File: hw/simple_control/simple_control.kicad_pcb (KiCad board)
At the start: 4 copper layers, 80 x 100 mm, 105 parts, among them J101 Screw_Terminal_01x02, J102 Jack-DC, J103 Screw_Terminal_01x03, J104 Screw_Terminal_01x03, J1301 Micro_SD_Card, J1401 Conn_02x05_Odd_Even, J601 Conn_01x04, J602 Raspberry_Pi_0_2_3, J603 Conn_01x03, Q1001 BC817, Q201 AOSP21357, Q701 BC817, Q801 BC817, Q901 BC817, SW1801 SW_Push, SW1901 SW_Push, SW2001 SW_Push, SW2101 SW_Push, SW602 SW_Push, U1101 CAT24C256, U1501 4050, U301 SN74AHCT125D, U601 PicoW

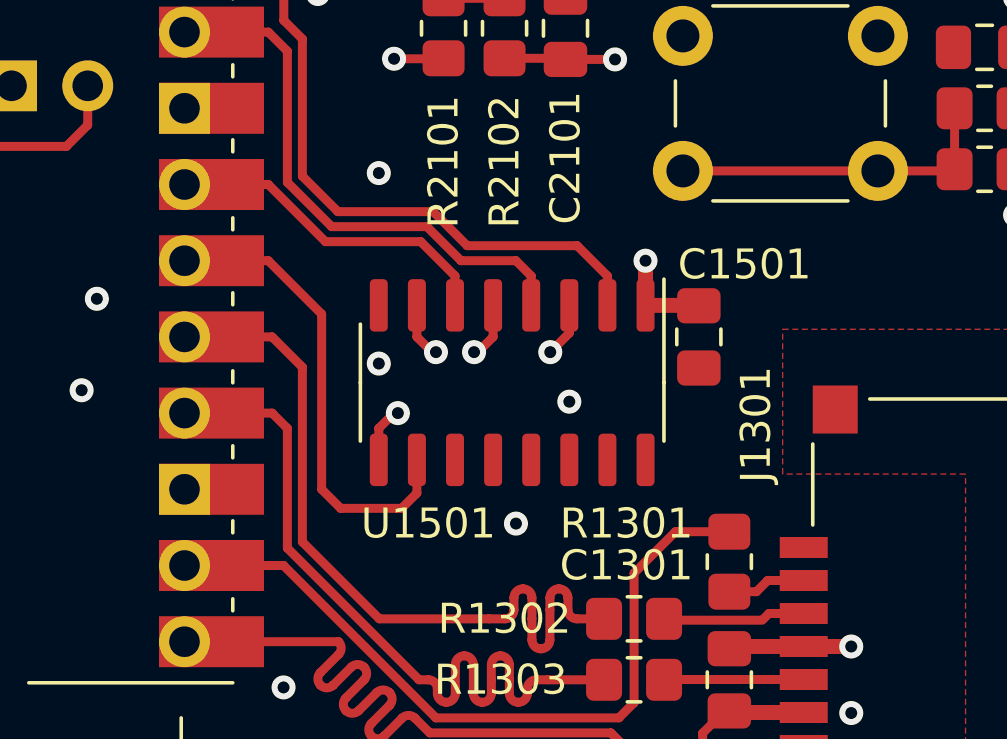
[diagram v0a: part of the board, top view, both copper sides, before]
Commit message: chore(hw): switch to 74AHC125 for keypad buffer
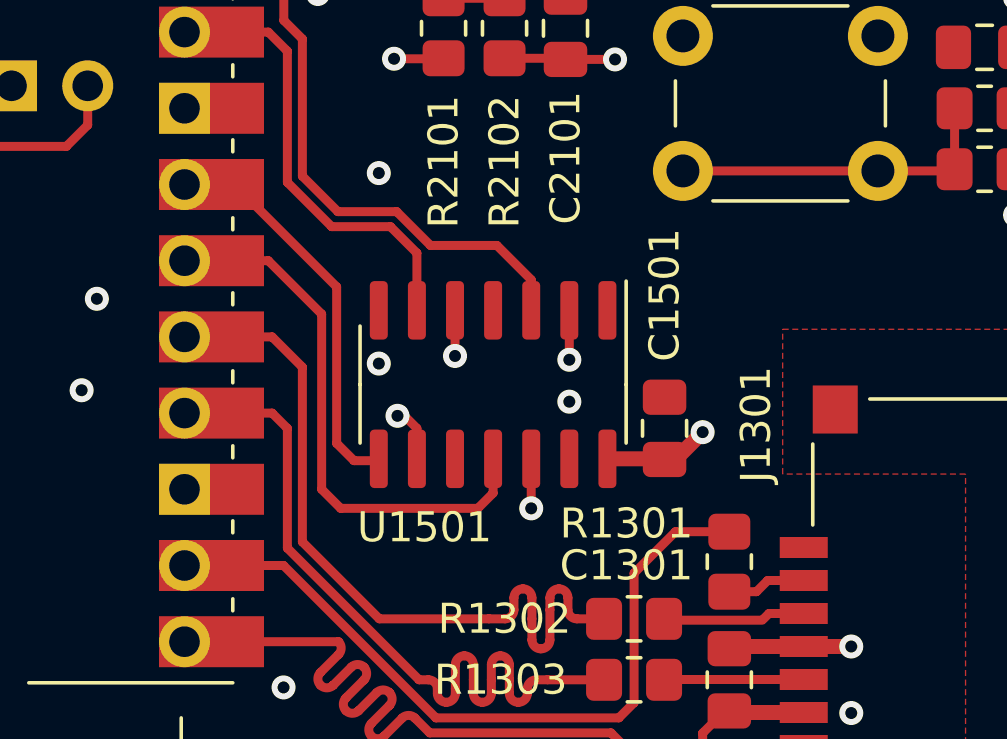
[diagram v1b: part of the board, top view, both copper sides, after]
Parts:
- U1501: value 4050 -> 74AHC125; footprint Package_SO:SO-16_3.9x9.9mm_P1.27mm -> Package_SO:SO-14_3.9x8.65mm_P1.27mm
- moved C1501 3.26 mm to (158.9, 96.3), turned to 90 degrees
- moved U1501 0.64 mm to (153.2, 94.8)
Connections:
- U1501 pad 1: +3.3V -> GND
- U1501 pad 10: /CPU/BUTTON3 -> GND
- U1501 pad 11: GND -> /CPU/BUTTON3
- U1501 pad 12: unconnected-(U1501-Pad12) -> /CPU/Keypad/Filtered Button 3/SW
- U1501 pad 13: (no net) -> GND
- U1501 pad 14: GND -> +3.3V
- U1501 pad 2: /CPU/BUTTON0 -> /CPU/Keypad/Filtered Button 0/SW
- U1501 pad 3: /CPU/Keypad/Filtered Button 0/SW -> /CPU/BUTTON0
- U1501 pad 4: /CPU/BUTTON1 -> GND
- U1501 pad 6: /CPU/BUTTON2 -> /CPU/BUTTON1
- U1501 pad 7: /CPU/Keypad/Filtered Button 2/SW -> GND
- U1501 pad 8: GND -> /CPU/BUTTON2
- U1501 pad 9: /CPU/Keypad/Filtered Button 3/SW -> /CPU/Keypad/Filtered Button 2/SW
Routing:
- net /CPU/Keypad/Filtered Button 3/SW: track 20.4 -> 27.6 mm
- net /CPU/BUTTON1: track 47.0 -> 43.9 mm
- net /CPU/Keypad/Filtered Button 2/SW: track 31.1 -> 33.7 mm
- net /CPU/BUTTON3: track 51.7 -> 54.2 mm
- net /CPU/BUTTON0: track 67.4 -> 65.0 mm
- net /CPU/BUTTON2: track 38.8 -> 40.8 mm
- net GND: vias 50 -> 49

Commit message: chore(hw): minor layout fixes, add notes
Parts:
- moved U1501 0.06 mm to (153.2, 94.9)
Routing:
- net GND: vias 49 -> 51

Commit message: chore(hw): improve layout
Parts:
- moved C1402 0.76 mm to (153.0, 48.1)
- moved C1401 0.63 mm to (153.0, 45.8)
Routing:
- net GND: track 110.1 -> 122.5 mm, vias 51 -> 53
- net /CPU/TERM_TXD: track 87.3 -> 97.6 mm
- net Net-(U301-3~{OE}): track 16.9 -> 21.6 mm
- net /CPU/TERM_RXD: track 82.8 -> 79.6 mm
- net +5V: track 49.4 -> 51.9 mm
- net Net-(U301-1~{OE}): track 19.7 -> 21.9 mm, vias 0 -> 2
- net /CPU/STAT_LED3: track 88.0 -> 89.2 mm
- net /LED_DATA_~{EN}0: track 85.8 -> 86.4 mm
- net /CPU/RTC_SDA: track 61.3 -> 61.9 mm
- net /CPU/RTC_SCL: track 66.0 -> 66.6 mm
- net /CPU/STAT_LED2: track 92.8 -> 93.4 mm
- net /CPU/STAT_LED1: track 82.4 -> 83.0 mm
- net /CPU/STAT_LED0: track 86.5 -> 87.1 mm
- net Net-(U301-3A): track 14.6 -> 14.2 mm, vias 2 -> 0
- net Net-(U301-1A): track 14.8 -> 15.0 mm, vias 2 -> 0

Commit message: chore(hw): add JLC order number
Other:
- board text added: "JLCJLCJLCJLC"
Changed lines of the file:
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@@
   (gr_line (start 108.1 140.64) (end 175.1 140.64)
     (stroke (width 0.1) (type default)) (layer "Edge.Cuts"))
+  (gr_text "JLCJLCJLCJLC" (at 158.369 132.207) (layer "F.SilkS")
+    (effects (font (size 1 1) (thickness 0.15)) (justify left bottom))
+  )
   (dimension (type aligned) (layer "Eco1.User")
     (pts (xy 108.1 40.64) (xy 108.1 140.64))

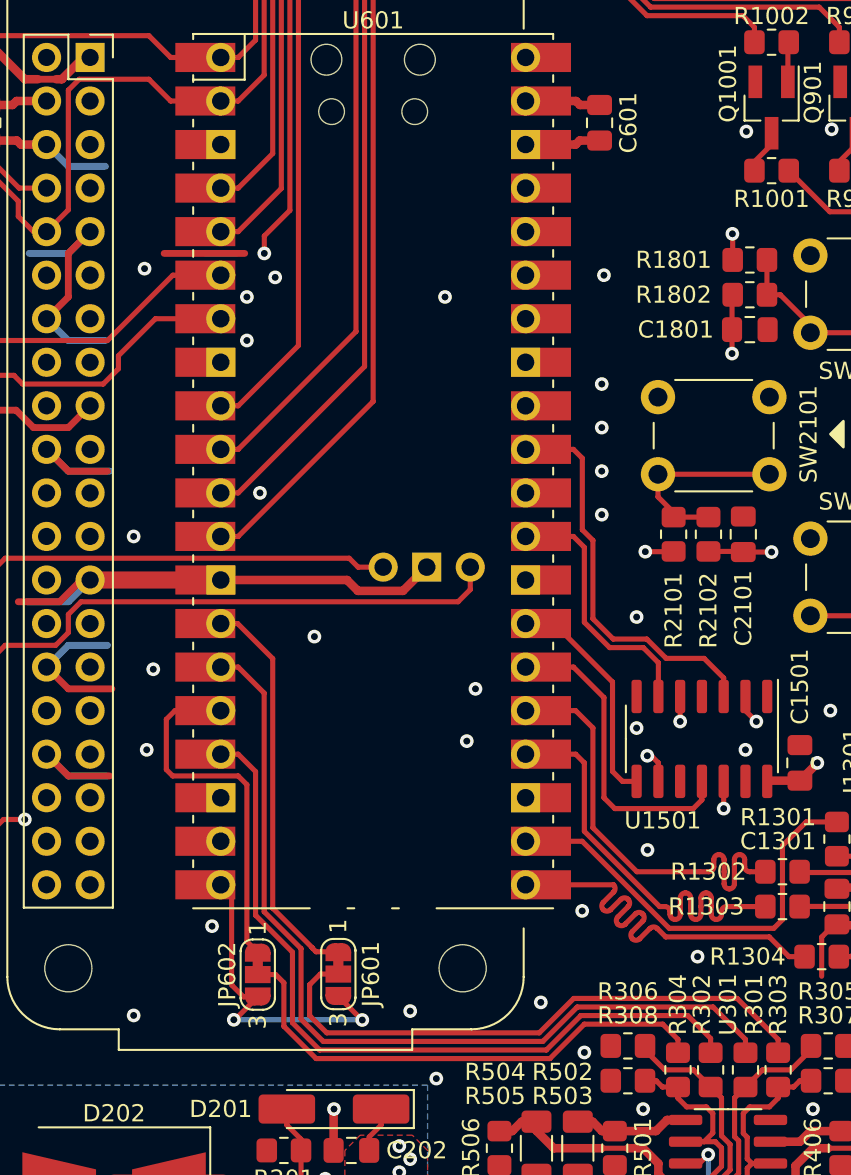
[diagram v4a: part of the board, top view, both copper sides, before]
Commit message: chore(hw): move LED data outside of antenna keep-out area
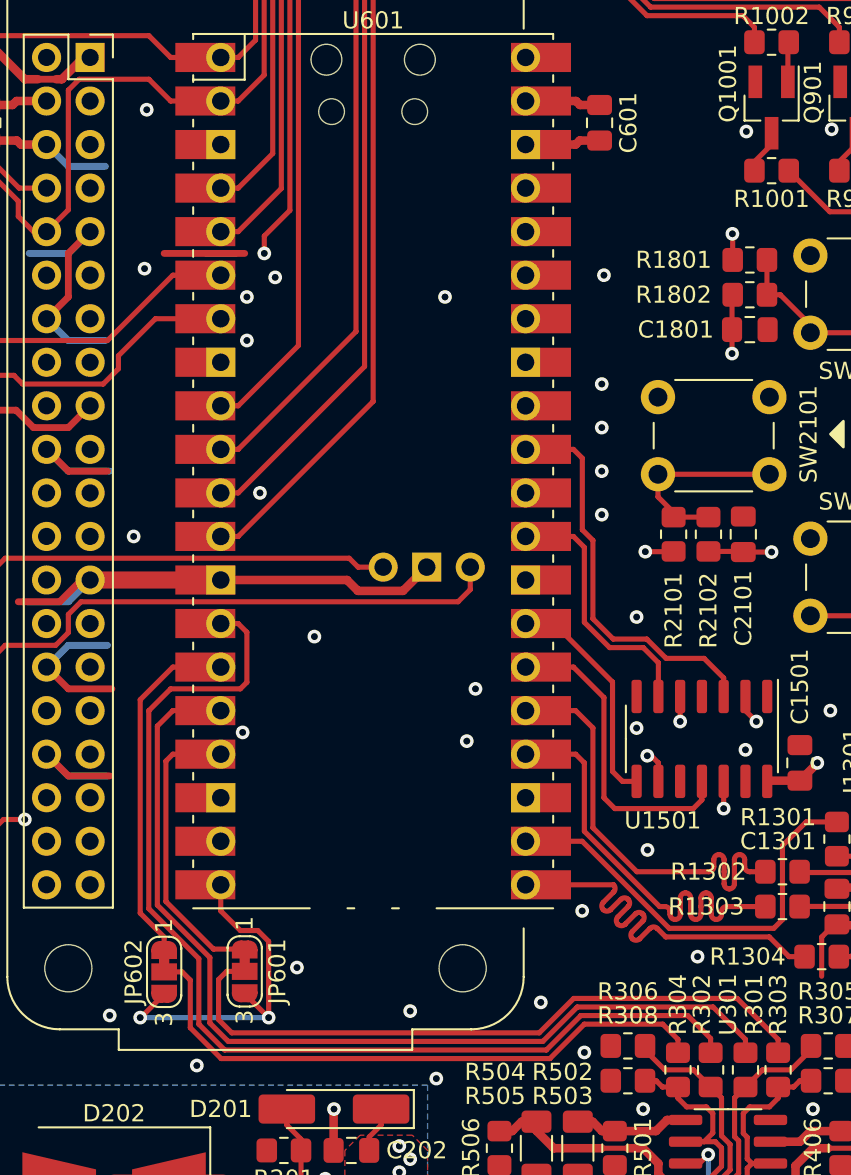
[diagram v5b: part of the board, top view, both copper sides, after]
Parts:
- moved JP601 5.46 mm to (126.5, 108.4)
- moved JP602 5.46 mm to (121.8, 108.5)
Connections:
- U601 pad 14: /CPU/PRIM_LED_DATA0 -> /LED_DATA_~{EN}1
- U601 pad 15: /LED_DATA_~{EN}0 -> /CPU/PRIM_LED_DATA1
- U601 pad 16: /CPU/PRIM_LED_DATA1 -> /LED_DATA_~{EN}0
- U601 pad 17: /LED_DATA_~{EN}1 -> /CPU/PRIM_LED_DATA0
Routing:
- net /LED_DATA_~{EN}1: track 56.5 -> 86.8 mm
- net /LED_DATA_~{EN}0: track 86.4 -> 93.8 mm
- net /LED_DATA1: track 30.0 -> 35.7 mm
- net /LED_DATA0: track 34.1 -> 39.6 mm
- net /CPU/PRIM_LED_DATA0: track 35.6 -> 30.7 mm
- net /CPU/PRIM_LED_DATA1: track 30.1 -> 34.0 mm
- net /CPU/ALT_LED_DATA: track 30.5 -> 32.1 mm
- net GND: vias 53 -> 54

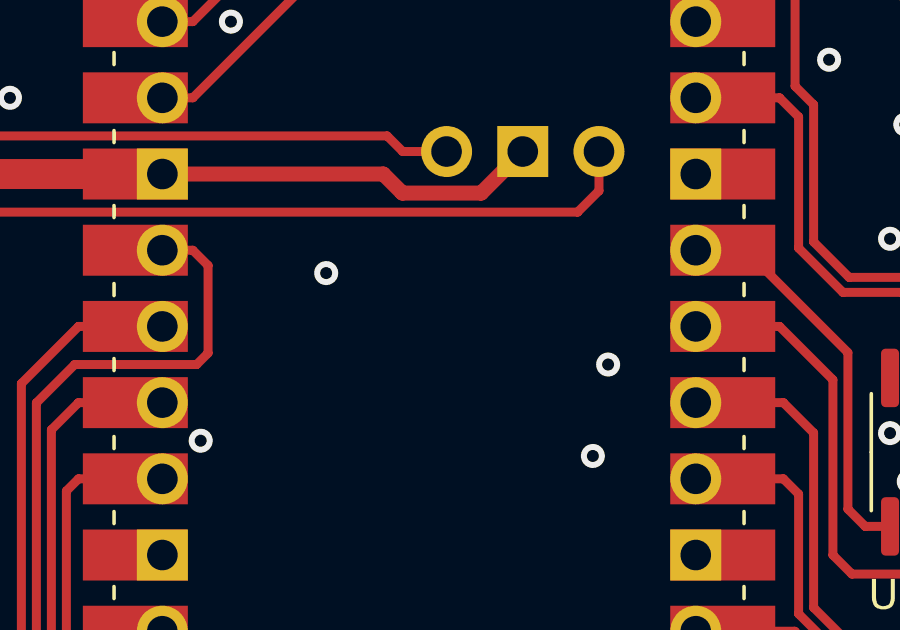
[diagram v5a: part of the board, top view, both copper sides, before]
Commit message: chore(hw): move vias under RPi
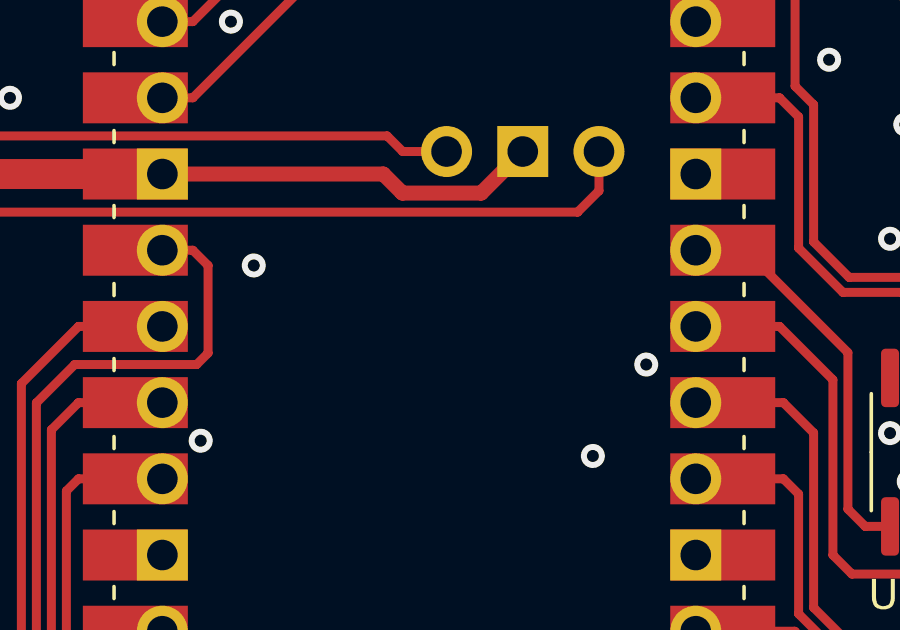
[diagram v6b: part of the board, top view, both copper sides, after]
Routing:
- net Net-(U601-RUN): track 54.1 -> 54.8 mm
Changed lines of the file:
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@@
   (via (at 165.1 105.7556) (size 0.8) (drill 0.4) (layers "F.Cu" "B.Cu") (free) (net 2))
   (via (at 165.6588 59.309) (size 0.8) (drill 0.4) (layers "F.Cu" "B.Cu") (free) (net 2))
-  (via (at 130.556 88.9) (size 0.8) (drill 0.4) (layers "F.Cu" "B.Cu") (free) (net 2))
+  (via (at 128.143 88.646) (size 0.8) (drill 0.4) (layers "F.Cu" "B.Cu") (free) (net 2))
   (via (at 162.814 77.089) (size 0.8) (drill 0.4) (layers "F.Cu" "B.Cu") (free) (net 2))
   (via (at 159.639 116.459) (size 0.8) (drill 0.4) (layers "F.Cu" "B.Cu") (free) (net 2))
@@
   (segment (start 113.665 99.568) (end 112.418 99.568) (width 0.3) (layer "F.Cu") (net 65))
   (segment (start 109.982 102.004) (end 109.982 95.504) (width 0.3) (layer "F.Cu") (net 65))
-  (via (at 139.954 91.948) (size 0.8) (drill 0.4) (layers "F.Cu" "B.Cu") (net 65))
+  (via (at 141.224 91.948055) (size 0.8) (drill 0.4) (layers "F.Cu" "B.Cu") (net 65))
   (via (at 113.665 99.568) (size 0.8) (drill 0.4) (layers "F.Cu" "B.Cu") (net 65))
   (segment (start 125.857 97.028) (end 123.825 97.028) (width 0.3) (layer "In1.Cu") (net 65))
-  (segment (start 139.954 91.948) (end 136.652 95.25) (width 0.3) (layer "In1.Cu") (net 65))
   (segment (start 123.825 97.028) (end 121.285 99.568) (width 0.3) (layer "In1.Cu") (net 65))
-  (segment (start 136.652 95.25) (end 127.300057 95.25) (width 0.3) (layer "In1.Cu") (net 65))
+  (segment (start 141.224 91.948055) (end 139.953945 91.948055) (width 0.3) (layer "In1.Cu") (net 65))
+  (segment (start 121.285 99.568) (end 113.665 99.568) (width 0.3) (layer "In1.Cu") (net 65))
+  (segment (start 126.492 96.393) (end 125.857 97.028) (width 0.3) (layer "In1.Cu") (net 65))
+  (segment (start 139.953945 91.948055) (end 136.652 95.25) (width 0.3) (layer "In1.Cu") (net 65))
   (segment (start 126.492 96.058057) (end 126.492 96.393) (width 0.3) (layer "In1.Cu") (net 65))
   (segment (start 127.300057 95.25) (end 126.492 96.058057) (width 0.3) (layer "In1.Cu") (net 65))
-  (segment (start 114.935 99.568) (end 113.665 99.568) (width 0.3) (layer "In1.Cu") (net 65))
-  (segment (start 126.492 96.393) (end 125.857 97.028) (width 0.3) (layer "In1.Cu") (net 65))
-  (segment (start 121.285 99.568) (end 114.935 99.568) (width 0.3) (layer "In1.Cu") (net 65))
-  (segment (start 139.954 91.948) (end 141.224 90.678) (width 0.3) (layer "In2.Cu") (net 65))
+  (segment (start 136.652 95.25) (end 127.300057 95.25) (width 0.3) (layer "In1.Cu") (net 65))
   (segment (start 141.224 81.153) (end 141.859 80.518) (width 0.3) (layer "In2.Cu") (net 65))
+  (segment (start 141.224 91.948055) (end 141.224 81.153) (width 0.3) (layer "In2.Cu") (net 65))
   (segment (start 141.859 80.518) (end 142.875 80.518) (width 0.3) (layer "In2.Cu") (net 65))
-  (segment (start 141.224 90.678) (end 141.224 81.153) (width 0.3) (layer "In2.Cu") (net 65))
   (segment (start 147.947 96.766) (end 148.525 97.344) (width 0.3) (layer "F.Cu") (net 66))
   (segment (start 142.875 88.138) (end 144.535 88.138) (width 0.3) (layer "F.Cu") (net 66))

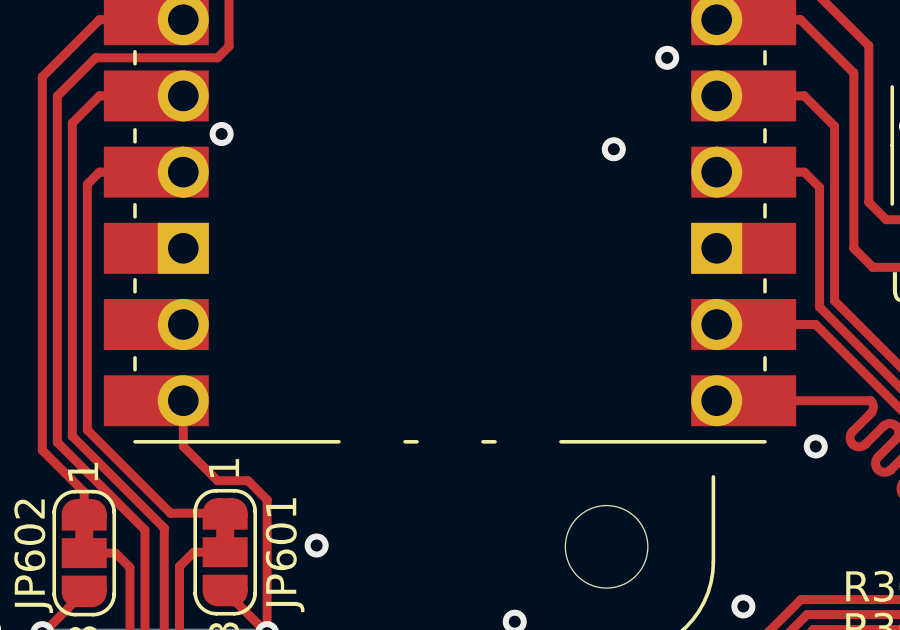
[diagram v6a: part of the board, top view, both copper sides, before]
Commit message: chore(hw): add hole for antenna
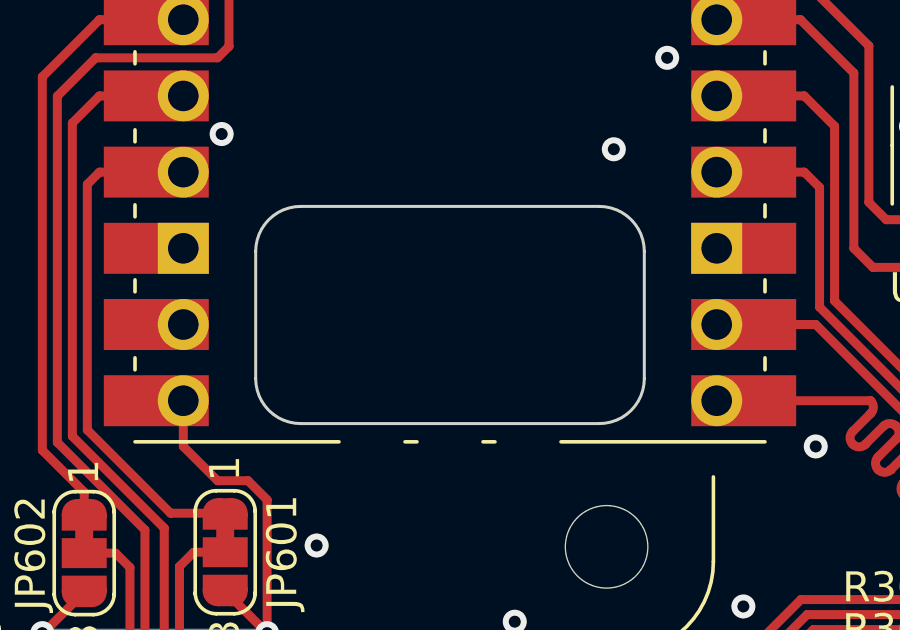
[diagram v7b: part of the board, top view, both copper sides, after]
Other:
- outline, holes or cut-outs redrawn
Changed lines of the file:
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@@
     )
     (stroke (width 0.15) (type solid)) (fill solid) (layer "F.SilkS"))
+  (gr_line (start 138.962 104.14) (end 129.008 104.14)
+    (stroke (width 0.1) (type default)) (layer "Edge.Cuts"))
   (gr_line (start 101.6 47.14) (end 101.6 134.14)
     (stroke (width 0.1) (type default)) (layer "Edge.Cuts"))
@@
   (gr_arc (start 108.1 140.64) (mid 103.503806 138.736194) (end 101.6 134.14)
     (stroke (width 0.1) (type default)) (layer "Edge.Cuts"))
+  (gr_arc (start 138.962 96.901) (mid 140.02266 97.34034) (end 140.462 98.401)
+    (stroke (width 0.1) (type default)) (layer "Edge.Cuts"))
   (gr_arc (start 181.6 134.14) (mid 179.696194 138.736194) (end 175.1 140.64)
     (stroke (width 0.1) (type default)) (layer "Edge.Cuts"))
@@
   (gr_line (start 175.1 40.64) (end 108.1 40.64)
     (stroke (width 0.1) (type default)) (layer "Edge.Cuts"))
+  (gr_arc (start 140.462 102.64) (mid 140.02266 103.70066) (end 138.962 104.14)
+    (stroke (width 0.1) (type default)) (layer "Edge.Cuts"))
   (gr_arc (start 101.6 47.14) (mid 103.503806 42.543806) (end 108.1 40.64)
     (stroke (width 0.1) (type default)) (layer "Edge.Cuts"))
   (gr_line (start 108.1 140.64) (end 175.1 140.64)
+    (stroke (width 0.1) (type default)) (layer "Edge.Cuts"))
+  (gr_line (start 129.008 96.901) (end 138.962 96.901)
+    (stroke (width 0.1) (type default)) (layer "Edge.Cuts"))
+  (gr_line (start 127.508 102.64) (end 127.508 98.401)
+    (stroke (width 0.1) (type default)) (layer "Edge.Cuts"))
+  (gr_arc (start 127.508 98.401) (mid 127.94734 97.34034) (end 129.008 96.901)
+    (stroke (width 0.1) (type default)) (layer "Edge.Cuts"))
+  (gr_arc (start 129.008 104.14) (mid 127.94734 103.70066) (end 127.508 102.64)
+    (stroke (width 0.1) (type default)) (layer "Edge.Cuts"))
+  (gr_line (start 140.462 98.401) (end 140.462 102.64)
     (stroke (width 0.1) (type default)) (layer "Edge.Cuts"))
   (gr_text "JLCJLCJLCJLC" (at 158.369 132.207) (layer "F.SilkS")
@@
     )
   )
-  (zone (net 0) (net_name "") (layers "F.Cu" "In1.Cu" "In2.Cu" "B.Cu") (hatch edge 0.5)
+  (zone (net 0) (net_name "") (layers "*.Adhes" "*.Paste" "*.SilkS" "*.Mask" "F.Cu" "In1.Cu" "In2.Cu" "B.Cu") (hatch edge 0.5)
     (connect_pads (clearance 0))
     (min_thickness 0.25) (filled_areas_thickness no)
